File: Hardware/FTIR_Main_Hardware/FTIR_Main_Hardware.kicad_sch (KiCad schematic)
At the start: 83 parts, among them J1 RJ45_LED_Shielded, Q1 IRF7606PBF, Q2 BSS138, Q3 IRF7606PBF, Q4 BSS138, Q5 IRF7606PBF, Q6 BSS138, U2 TMC2208, U3 TSR_1-2450, U6 Peensy4.1_DEV-16771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

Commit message: Updating from review
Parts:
- removed R11: 50, symbol Device:R
- removed R12: 40, symbol Device:R
- removed U3: TSR_1-2450, Converter_DCDC:Converter_DCDC_TRACO_TSR-1_THT, symbol Regulator_Switching:TSR_1-2450
- added U3: OKI, symbol MRDT_Devices:OKI
- C14: value Ccomp -> 100pF
- R1: value 23 -> 230
- R10: value 100 -> 330
- R17: value Rs -> 6
- R2: value 10 -> 100
- R23: value 10k -> 5k
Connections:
- net 2.2v_Divider is gone; now on net +5V: C12.1, U5. (VREF_OUT)
- net +12V: now also C15.1, U7.1 (Vi), U3.1 (Vi)
- net +3V3: now also Q3.1 (S), Q3.2 (S), Q3.3 (S), R22.1, U1.5 (V+), U4.5 (V+); no longer U1.2 (V-), U4.2 (V-)
- net +5V: now also U3.3 (Vo); no longer C15.1, Q3.1 (S), Q3.2 (S), Q3.3 (S), R22.1, U7.1 (Vi)
- net GND: now also U1.2 (V-), U4.2 (V-), U3.2 (GND); no longer U1.5 (V+), U4.5 (V+)
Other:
- note added: "OKI for TIAs"
- moved on the sheet: C15, C16, C8, Conn10, Conn11, Conn12, Conn13, Conn3, Conn6, Conn8, Conn9, D2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

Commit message: Continuing review changes
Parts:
- removed LD1: D_Laser_Photo_PType, symbol Device:D_Laser_Photo_PType
- added LD1: D_Laser_Photo_NType, symbol Device:D_Laser_Photo_NType
- C12: value Cin -> 100uF
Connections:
- net DIAG: now also U6.26 (A12)
- net DIR: now also U6.40 (A16)
- net INDEX: now also U6.25 (A11)
- net STEP: now also U6.41 (A17)
- net UART: now also U6.27 (A13)
- net at R17.2: now also LD1.2
- new net: LD1.1, U5. (VREF_OUT)
- new net: LD1.3, U5. (VREF_OUT)
- no-connect marks 46 -> 39
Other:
- moved on the sheet: R17

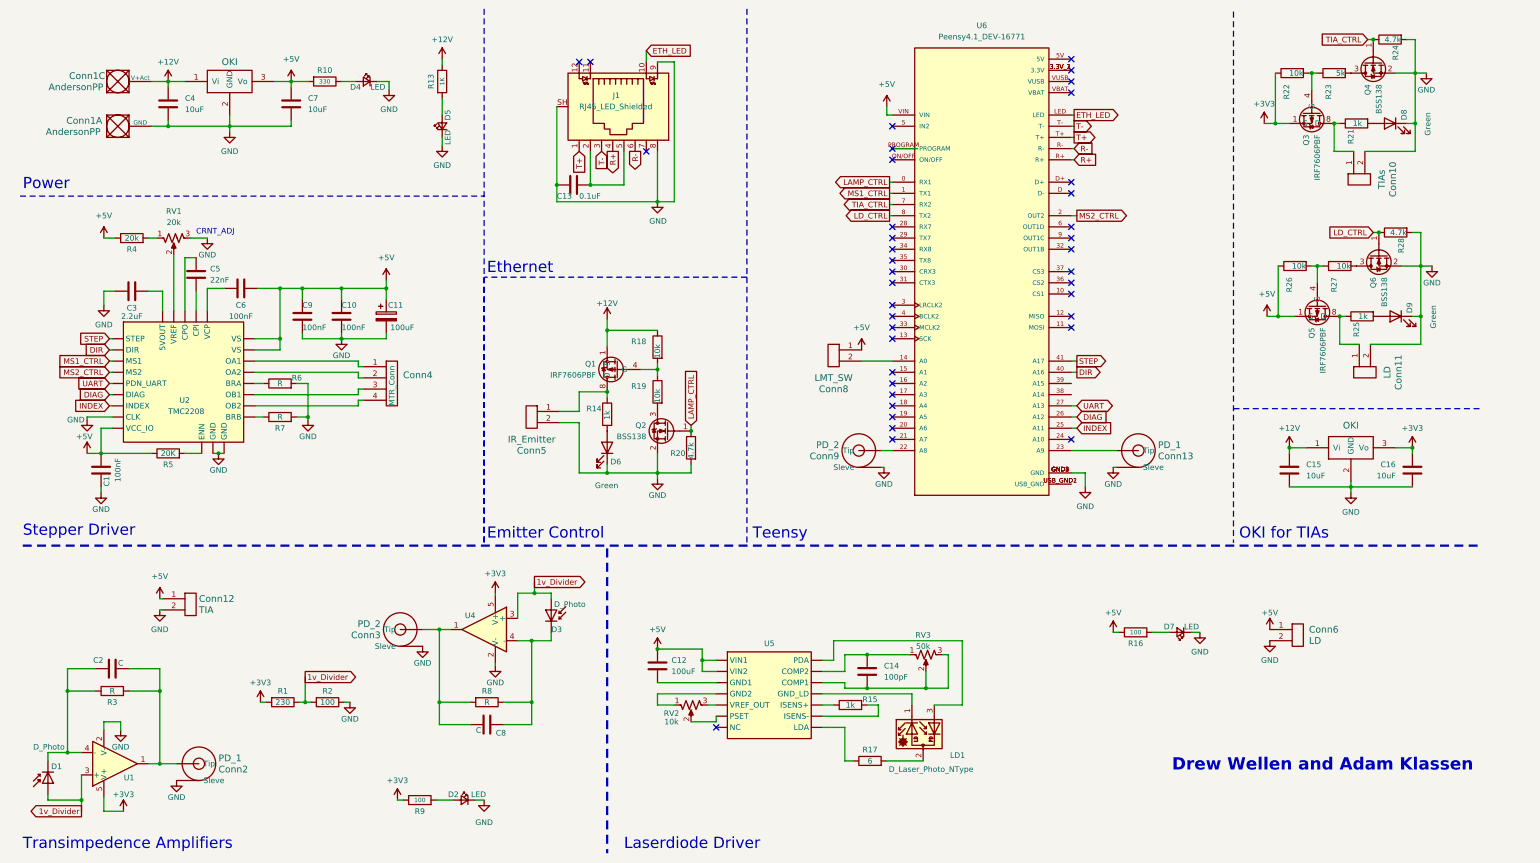
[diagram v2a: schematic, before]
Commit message: Figured out the op amps somewhat
now uses dual op amps and the capacitance is calculated on one of them
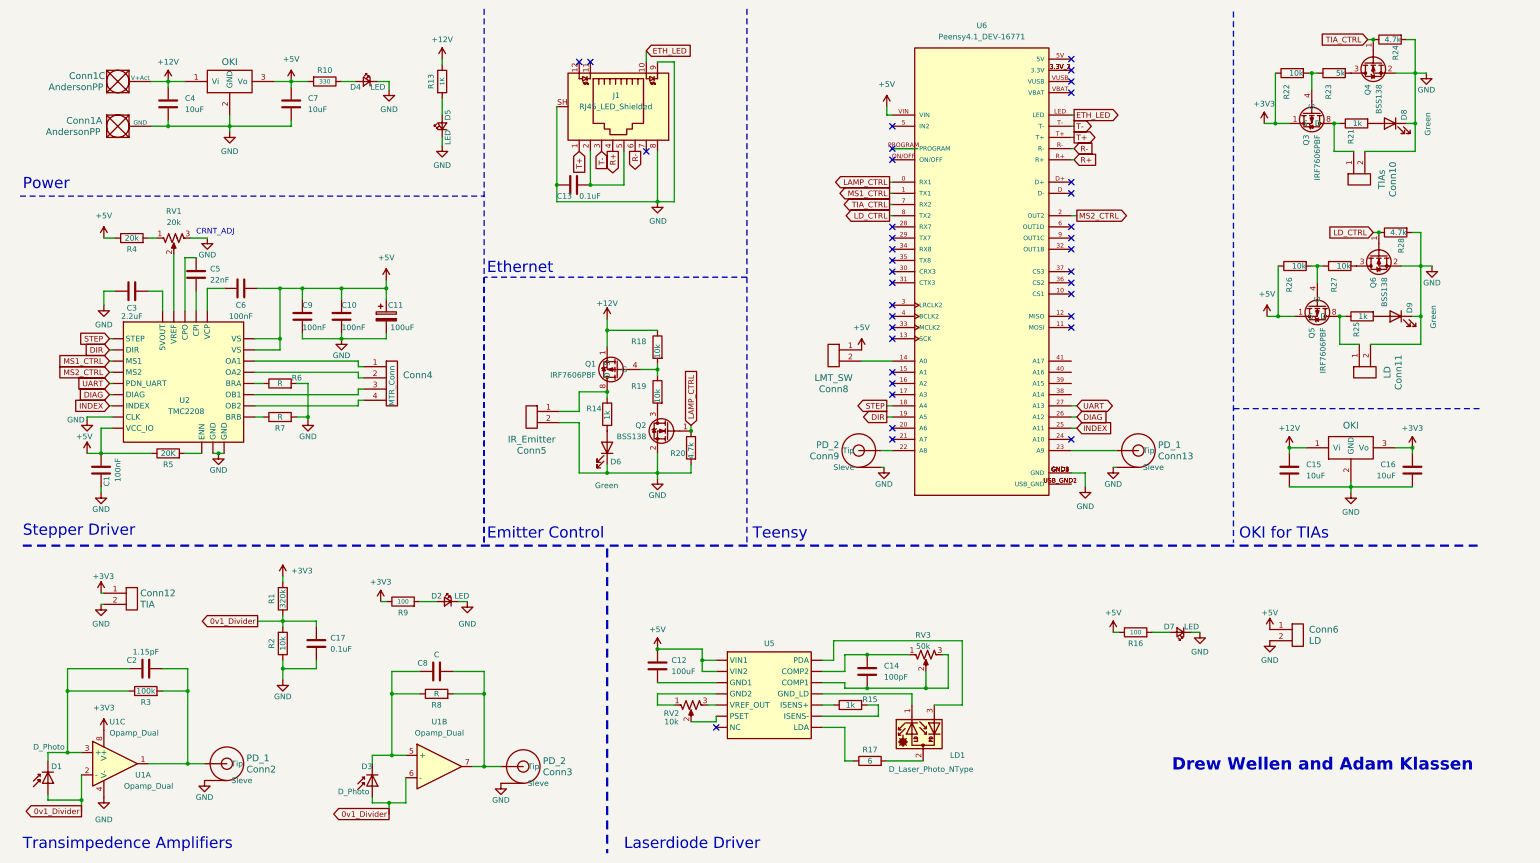
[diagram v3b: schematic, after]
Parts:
- removed U1, U4: ~, symbol Amplifier_Operational:ADA4610-1xRJ
- added C17: 0.1uF, symbol Device:C
- added U1: Opamp_Dual, symbol Device:Opamp_Dual
- C2: value C -> 1.15pF
- R1: value 230 -> 320k
- R2: value 100 -> 10k
- R3: value R -> 100k
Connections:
- net +3V3: now also Conn12.1, U1.8 (V+)
- net +5V: no longer Conn12.1
- net DIR: now also U6.19 (A5); no longer U6.40 (A16)
- net GND: now also C17.2, U1.4 (V-)
- net STEP: now also U6.18 (A4); no longer U6.41 (A17)
- net at C2.1, D1.1 (K), R3.1: now also U1.3 (+)
- net at C2.2, Conn2.1 (Tip), R3.2: now also U1.1
- net at C8.1, D3.1 (K), R8.1: now also U1.5 (+)
- net at C8.2, Conn3.1 (Tip), R8.2: now also U1.7
- net 1v_Divider renamed 0v1_Divider
- net 0v1_Divider: now also C17.1, U1.2 (-), U1.6 (-)
- no-connect marks 39 -> 37
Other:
- moved on the sheet: C2, C8, Conn12, Conn2, Conn3, D2, D3, R1, R2, R3, R8, R9

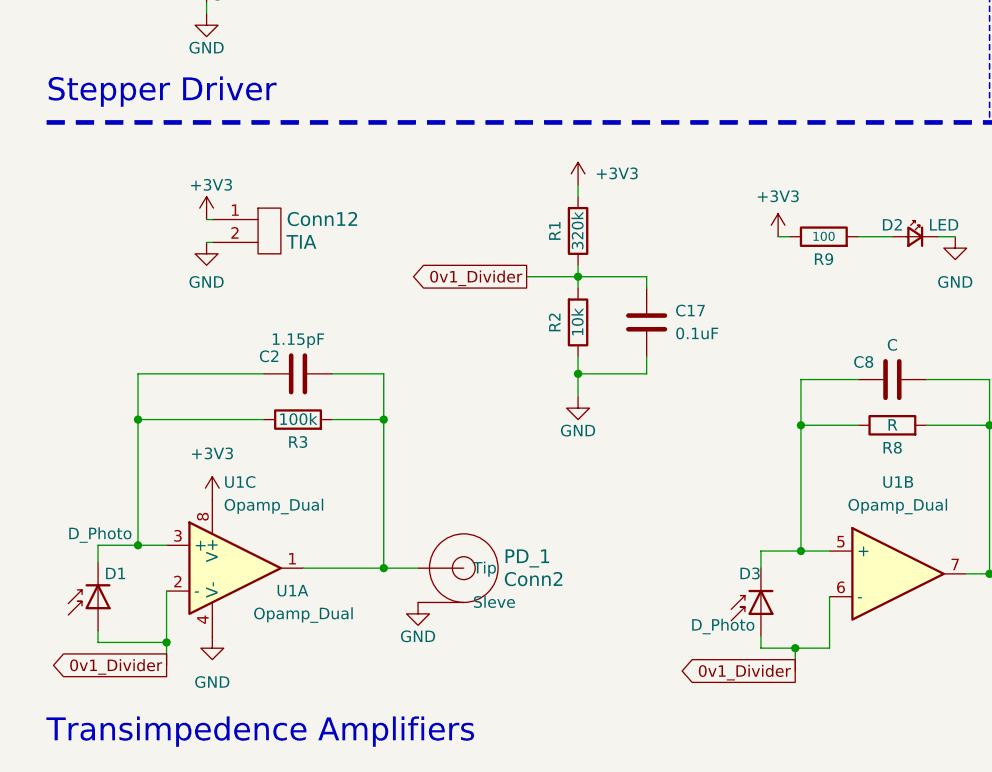
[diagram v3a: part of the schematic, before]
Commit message: Changes to TIA
Set reference voltage to ground and removed the voltage divider altogether
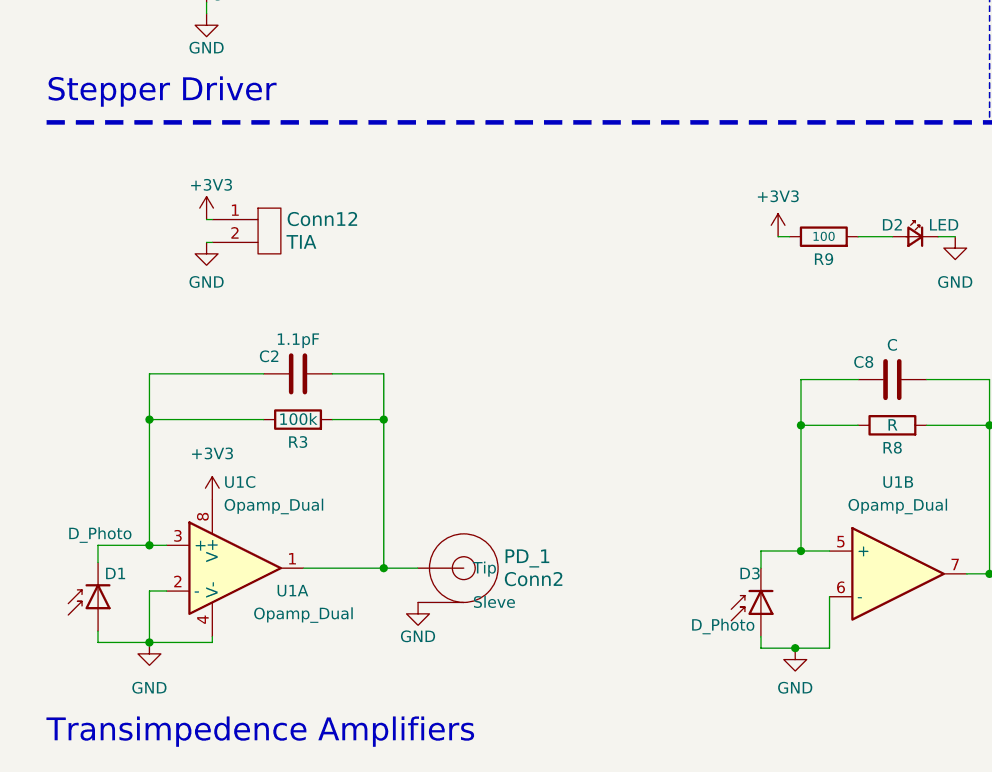
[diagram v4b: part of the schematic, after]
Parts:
- removed C17: 0.1uF, symbol Device:C
- removed R1: 320k, symbol Device:R
- removed R2: 10k, symbol Device:R
- C2: value 1.15pF -> 1.1pF
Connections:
- net 0v1_Divider is gone; now on net GND: D1.2 (A), D3.2 (A), U1.2 (-), U1.6 (-)

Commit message: Malacki changes
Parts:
- C2: value 1.1pF -> C
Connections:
- net GND: now also U1.3 (+), U1.5 (+); no longer U1.2 (-), U1.6 (-)
- net at C2.1, D1.1 (K), R3.1: now also U1.2 (-); no longer U1.3 (+)
- net at C8.1, D3.1 (K), R8.1: now also U1.6 (-); no longer U1.5 (+)
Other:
- moved on the sheet: C2, Conn2, D1, R3, U1A, U1C

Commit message: Value changes
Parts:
- R10: value 330 -> 300
- R16: value 100 -> 300
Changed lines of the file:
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@@
     (stroke (width 0) (type default))
   )
+  (wire (pts (xy 294.64 153.035) (xy 295.91 153.035))
+    (stroke (width 0) (type default))
+  )
   (wire (pts (xy 117.475 162.56) (xy 117.475 167.64))
     (stroke (width 0) (type default))
@@
     (stroke (width 0) (type default))
   )
+  (wire (pts (xy 294.64 155.575) (xy 295.91 155.575))
+    (stroke (width 0) (type default))
+  )
   (wire (pts (xy 102.87 146.685) (xy 106.68 146.685))
     (stroke (width 0) (type default))
@@
     (stroke (width 0) (type default))
   )
+  (wire (pts (xy 204.47 89.535) (xy 203.2 89.535))
+    (stroke (width 0) (type default))
+  )
   (wire (pts (xy 77.47 104.775) (xy 77.47 105.41))
     (stroke (width 0) (type default))
@@
       (effects (font (size 1.27 1.27)))
     )
-    (property "Value" "330" (at 81.28 28.575 90)
+    (property "Value" "300" (at 81.28 28.575 90)
       (effects (font (size 0.9906 0.9906)))
     )
@@
     )
   )
-  (symbol (lib_id "power:GND") (at 295.91 155.575 0) (unit 1)
+  (symbol (lib_id "power:GND") (at 294.64 155.575 0) (unit 1)
     (in_bom yes) (on_board yes) (dnp no) (fields_autoplaced)
-    (property "Reference" "#PWR030" (at 295.91 161.925 0)
+    (property "Reference" "#PWR030" (at 294.64 161.925 0)
       (effects (font (size 1.27 1.27)) hide)
     )
-    (property "Value" "GND" (at 295.91 160.02 0)
+    (property "Value" "GND" (at 294.64 160.02 0)
       (effects (font (size 1.27 1.27)))
     )
-    (property "Footprint" "" (at 295.91 155.575 0)
+    (property "Footprint" "" (at 294.64 155.575 0)
       (effects (font (size 1.27 1.27)) hide)
     )
-    (property "Datasheet" "" (at 295.91 155.575 0)
+    (property "Datasheet" "" (at 294.64 155.575 0)
       (effects (font (size 1.27 1.27)) hide)
     )
@@
     )
   )
-  (symbol (lib_id "power:+5V") (at 295.91 153.035 0) (unit 1)
+  (symbol (lib_id "power:+5V") (at 294.64 153.035 0) (unit 1)
     (in_bom yes) (on_board yes) (dnp no)
-    (property "Reference" "#PWR029" (at 295.91 156.845 0)
+    (property "Reference" "#PWR029" (at 294.64 156.845 0)
       (effects (font (size 1.27 1.27)) hide)
     )
-    (property "Value" "+5V" (at 295.91 149.225 0)
+    (property "Value" "+5V" (at 294.64 149.225 0)
       (effects (font (size 1.27 1.27)))
     )
-    (property "Footprint" "" (at 295.91 153.035 0)
+    (property "Footprint" "" (at 294.64 153.035 0)
       (effects (font (size 1.27 1.27)) hide)
     )
-    (property "Datasheet" "" (at 295.91 153.035 0)
+    (property "Datasheet" "" (at 294.64 153.035 0)
       (effects (font (size 1.27 1.27)) hide)
     )
@@
     )
   )
-  (symbol (lib_id "power:+5V") (at 203.2 89.535 0) (unit 1)
+  (symbol (lib_id "power:+5V") (at 204.47 89.535 0) (unit 1)
     (in_bom yes) (on_board yes) (dnp no) (fields_autoplaced)
-    (property "Reference" "#PWR038" (at 203.2 93.345 0)
+    (property "Reference" "#PWR038" (at 204.47 93.345 0)
       (effects (font (size 1.27 1.27)) hide)
     )
-    (property "Value" "+5V" (at 203.2 84.455 0)
+    (property "Value" "+5V" (at 204.47 84.455 0)
       (effects (font (size 1.27 1.27)))
     )
-    (property "Footprint" "" (at 203.2 89.535 0)
+    (property "Footprint" "" (at 204.47 89.535 0)
       (effects (font (size 1.27 1.27)) hide)
     )
-    (property "Datasheet" "" (at 203.2 89.535 0)
+    (property "Datasheet" "" (at 204.47 89.535 0)
       (effects (font (size 1.27 1.27)) hide)
     )
@@
       (effects (font (size 1.27 1.27)))
     )
-    (property "Value" "100" (at 265.43 153.67 90)
+    (property "Value" "300" (at 265.43 153.67 90)
       (effects (font (size 0.9906 0.9906)))
     )

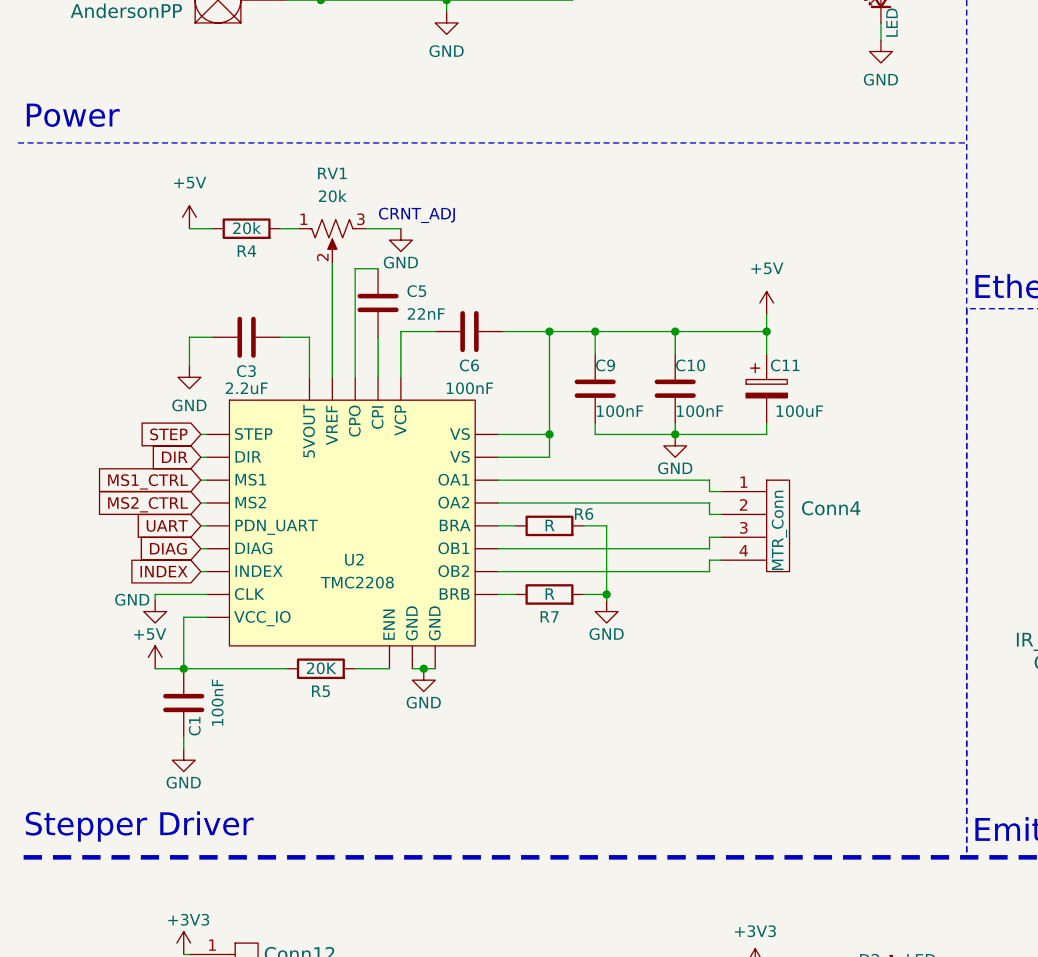
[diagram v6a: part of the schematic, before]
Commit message: Symbol for stepper
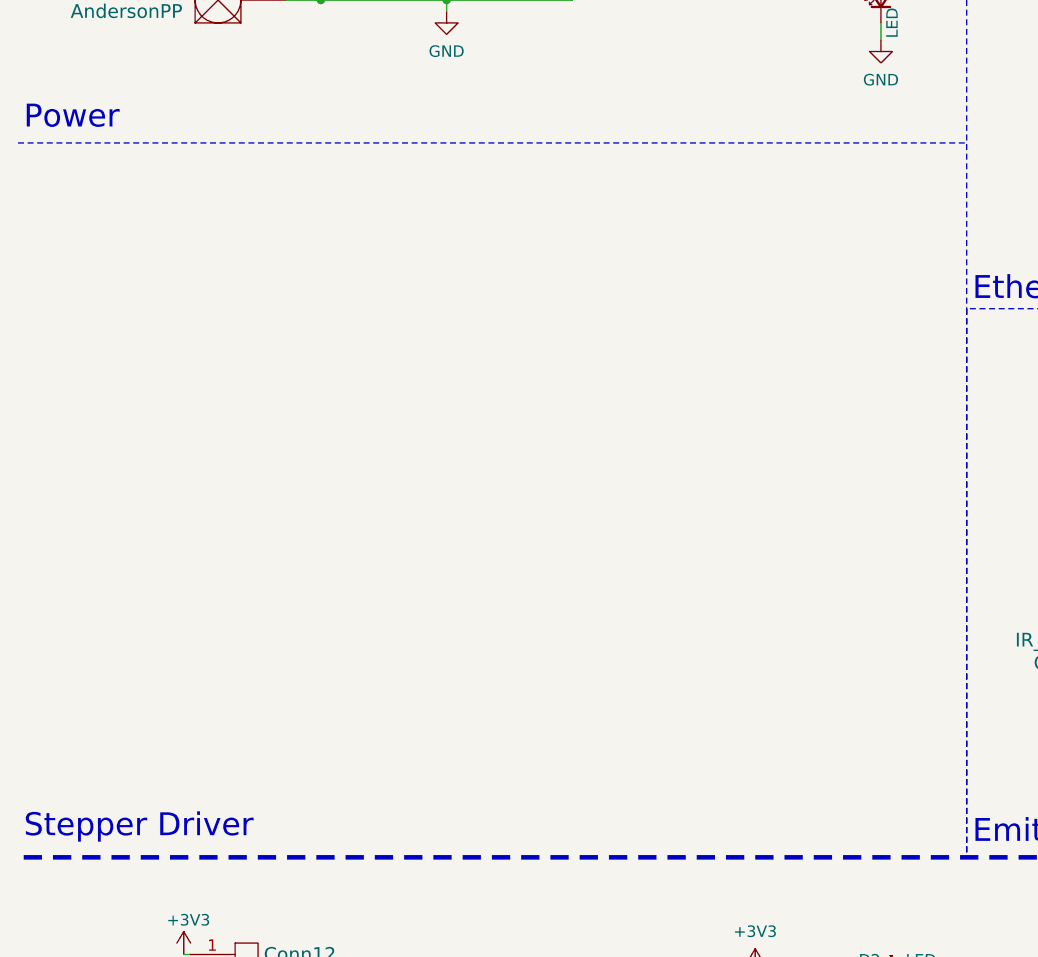
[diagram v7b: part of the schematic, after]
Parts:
- removed C1, C10, C6, C9: 100nF, symbol Device:C
- removed C11: 100uF, symbol Device:C_Polarized
- removed C3: 2.2uF, symbol Device:C
- removed C5: 22nF, symbol Device:C
- removed Conn4: MTR_Conn, symbol MRDT_Connectors:Molex_SL_04
- removed R4: 20k, symbol Device:R
- removed R5: 20K, symbol Device:R
- removed R6, R7: R, symbol Device:R
- removed RV1: 20k, symbol Device:R_Potentiometer_US
- removed U2: TMC2208, symbol MRDT_Devices:TMC2208
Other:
- note removed: "CRNT_ADJ"
